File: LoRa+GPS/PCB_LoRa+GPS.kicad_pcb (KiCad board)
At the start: 4 copper layers, 66 parts, among them J1 Conn_Coaxial_Small, J2 USB_C_Receptacle_USB2.0_16P, J4 Conn_Coaxial_Small, Q2 SS8050, Q3 AO3400A, Q4 SS8050, SW1 SW_Push, U1 ESP32-PICO-D4, U2 RFM95W-915S2, U3 TPS62A01ADRL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

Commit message: Add files via upload
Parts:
- added SW2: SW_SPST, Button_Switch_THT:SW_E-Switch_EG1271_SPDT, F.Cu at (85.0, 35.8)
- BT2: moved to B.Cu
- J1: footprint Connector_Coaxial:U.FL_Molex_MCRF_73412-0110_Vertical -> Connector_Coaxial:U.FL_Hirose_U.FL-R-SMT-1_Vertical
- SW1: footprint Button_Switch_SMD:SW_Push_1P1T_NO_Vertical_Wuerth_434133025816 -> Button_Switch_SMD:SW_Push_1P1T_NO_CK_KMR2
- moved Q4 102.1 mm to (61.9, 39.7)
- moved AJ-SR04M1 97.8 mm to (71.0, 36.0)
- moved Q2 87.3 mm to (61.0, 51.1), turned to -90 degrees
- moved U1 83.3 mm to (68.3, 46.3), turned to 180 degrees
- moved Q3 78.1 mm to (77.9, 36.0)
- moved C1 77.5 mm to (82.0, 61.8), turned to -90 degrees
- moved C6 71.9 mm to (69.0, 54.5), turned to -90 degrees
- moved C14 71.9 mm to (79.5, 61.8), turned to -90 degrees
- moved SW1 70.8 mm to (64.0, 60.8), turned to 180 degrees
- moved C4 70.6 mm to (62.5, 54.0)
- moved C11 70.0 mm to (66.5, 54.5), turned to -90 degrees
- moved C9 69.7 mm to (38.5, 43.0), turned to 180 degrees
- moved C15 68.8 mm to (76.9, 61.8), turned to -90 degrees
- moved C2 66.0 mm to (67.8, 54.5), turned to -90 degrees
- moved C3 65.0 mm to (66.5, 57.5), turned to 90 degrees
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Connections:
- BT2 pad 1: +BATT -> Net-(BT2-+)
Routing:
- net 3V3: track 0.00 -> 148.0 mm, vias 0 -> 7
- net GND: track 0.00 -> 76.0 mm, vias 0 -> 9
- net +BATT: track 0.00 -> 60.1 mm, vias 0 -> 1
- net VBUS: track 0.00 -> 53.2 mm, vias 0 -> 2
- net 5V: track 0.00 -> 52.7 mm, vias 0 -> 2
- net PPS_GPS: track 0.00 -> 40.6 mm, vias 0 -> 2
- net Rx_GPS: track 0.00 -> 39.5 mm, vias 0 -> 2
- net Net-(J4-In): track 0.00 -> 37.3 mm
- net Net-(U6-VBUS): track 0.00 -> 36.4 mm, vias 0 -> 3
- net Reset_LoRa: track 0.00 -> 35.6 mm, vias 0 -> 2
- net Tx_GPS: track 0.00 -> 34.4 mm, vias 0 -> 2
- net Net-(U3-SW): track 0.00 -> 33.6 mm, vias 0 -> 2
- net USB_D-: track 0.00 -> 31.6 mm, vias 0 -> 2
- net USB_D+: track 0.00 -> 28.6 mm, vias 0 -> 2
- net RX/TXdone_LoRa: track 0.00 -> 27.3 mm, vias 0 -> 2
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- added copper zone on B.Cu, net GND
- added copper zone on F.Cu, net GND
- added copper zone on In1.Cu, net GND
- added copper zone on In2.Cu, net GND
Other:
- board outline added: 80 x 40 mm

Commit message: Add files via upload
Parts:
- moved C8 25.8 mm to (32.5, 60.5), turned to 90 degrees
- moved C11 11.8 mm to (74.5, 63.3), turned to 90 degrees
- moved C13 11.8 mm to (80.5, 63.3)
- moved C12 11.5 mm to (79.0, 63.3)
- moved C10 11.3 mm to (77.5, 63.3)
- moved C3 11.1 mm to (76.0, 63.3)
- moved C2 10.2 mm to (73.0, 63.3), turned to 90 degrees
- moved R6 10.1 mm to (45.5, 45.0), turned to -90 degrees
- moved C4 9.50 mm to (62.5, 63.5)
- moved C6 9.12 mm to (71.5, 63.3), turned to 90 degrees
- moved R1 8.49 mm to (81.0, 36.0), turned to 90 degrees
- moved R15 5.08 mm to (52.5, 42.0), turned to 90 degrees
- moved R5 4.62 mm to (50.5, 40.5), turned to 0 degrees
- moved C16 4.51 mm to (70.5, 66.5)
- moved C7 4.51 mm to (73.0, 66.4)
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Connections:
- R18 pad 2: +3.3V -> 3V3
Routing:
- net U0TX_uC: track 1.17 -> 80.1 mm, vias 1 -> 3
- net GND: track 76.0 -> 13.1 mm, vias 9 -> 5
- net 3V3: track 148.0 -> 209.8 mm, vias 7 -> 8
- net uC_EN: track 25.0 -> 55.5 mm, vias 2 -> 3
- net Reset_LoRa: track 35.6 -> 57.4 mm, vias 2 -> 3
- net SCK_LoRa: track 19.8 -> 40.8 mm
- net Net-(U6-VBUS): track 36.4 -> 18.0 mm
- net 5V: track 52.7 -> 36.1 mm, vias 2 -> 1
- net NSS_LoRa: track 19.0 -> 34.6 mm
- net RX/TXdone_LoRa: track 27.3 -> 38.6 mm
- net Net-(U3-PG): track 4.72 -> 14.5 mm, vias 0 -> 2
- net U0RX_uC: track 24.3 -> 32.8 mm
- net USB_D+: track 28.6 -> 37.1 mm
- net MOSI_LoRa: track 14.1 -> 21.2 mm
- net Net-(U1-IO2): track 4.13 -> 8.25 mm
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
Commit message: Add files via upload
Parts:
- moved C13 43.8 mm to (38.5, 50.8), turned to 180 degrees
- moved C9 43.2 mm to (81.0, 35.0), turned to -90 degrees
- moved C12 41.9 mm to (38.5, 52.2), turned to 180 degrees
- moved C10 40.1 mm to (38.5, 53.7), turned to 180 degrees
- moved C7 36.4 mm to (52.8, 36.2), turned to 90 degrees
- moved C3 27.5 mm to (66.5, 37.5), turned to 180 degrees
- moved C6 25.9 mm to (68.8, 37.5), turned to 180 degrees
- moved C2 25.4 mm to (66.5, 38.8), turned to 180 degrees
- moved C11 25.2 mm to (68.8, 38.8), turned to 180 degrees
- moved R22 23.1 mm to (68.0, 57.5), turned to -90 degrees
- moved C1 20.2 mm to (100.0, 59.2), turned to 0 degrees
- moved C14 14.2 mm to (74.0, 52.8)
- moved C15 14.0 mm to (72.2, 52.8)
- moved U6 12.6 mm to (44.5, 48.5)
- moved C5 11.8 mm to (49.2, 42.5)
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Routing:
- net U0TX_uC: track 80.1 -> 7.38 mm, vias 3 -> 0
- net Net-(U6-RXD): track 5.60 -> 46.8 mm, vias 0 -> 2
- net USB_D+: track 37.1 -> 12.8 mm, vias 2 -> 0
- net USB_D-: track 33.9 -> 13.2 mm, vias 2 -> 0
- net Net-(U6-TXD): track 7.58 -> 26.1 mm, vias 0 -> 2
- net Net-(Q4-E): track 16.1 -> 31.4 mm
- net Net-(J4-In): track 37.3 -> 51.8 mm
- net Net-(Q2-E): track 18.6 -> 30.0 mm, vias 0 -> 3
- net Net-(Q2-B): track 21.0 -> 9.76 mm
- net GND: track 13.1 -> 22.2 mm, vias 5 -> 8
- net Net-(U4-ISET): track 9.54 -> 2.44 mm
- net Net-(J2-CC2): track 17.1 -> 10.3 mm, vias 0 -> 1
- net Net-(U4-ILIM): track 10.4 -> 3.95 mm
- net Net-(U4-TS): track 10.8 -> 4.64 mm
- net Net-(U4-ITERM): track 9.45 -> 3.44 mm
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
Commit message: Add files via upload
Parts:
- added BT1: 1056TR, CR1220 socket:BAT_1056TR, B.Cu at (75.5, 71.5)
- added R25: 10k, Resistor_SMD:R_0402_1005Metric, F.Cu at (49.5, 69.5)
- moved J4 37.4 mm to (38.5, 73.5)
- moved R24 23.5 mm to (78.5, 61.0), turned to 0 degrees
- moved C19 23.5 mm to (74.5, 44.0), turned to 45 degrees
- moved C4 11.3 mm to (73.5, 61.0)
- moved SW1 10.9 mm to (74.0, 65.2)
- moved R16 8.63 mm to (45.5, 52.0)
- moved CR1 8.44 mm to (32.0, 65.0), turned to -90 degrees
- moved J1 5.59 mm to (94.5, 69.0)
- moved C20 4.40 mm to (57.8, 54.0)
- moved C8 3.16 mm to (31.5, 57.5), turned to 0 degrees
- moved U5 2.28 mm to (49.3, 60.9)
- moved C3 1.44 mm to (65.5, 38.5), turned to 90 degrees
- moved C11 1.25 mm to (70.0, 38.5), turned to 90 degrees
- moved C6 1.06 mm to (68.5, 38.5), turned to 90 degrees
- moved C2 0.53 mm to (67.0, 38.5), turned to 90 degrees
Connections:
- C20 pad 2: Net-(U5-VBATT) -> Net-(U5-VCC)
- J1 pad 1: GND -> Net-(J1-In)
- J1 pad 2: Net-(J1-Ext) -> GND
- L2 pad 2: Net-(U5-VBATT) -> Net-(U5-VCC)
- U1 pad 20: unconnected-(U1-IO13-Pad20) -> Wake_GPS
- U1 pad 42: unconnected-(U1-IO21-Pad42) -> AntOff_GPS
- U2 pad 9: Net-(J1-Ext) -> Net-(J1-In)
- U5 pad 13: unconnected-(U5-ANT_OFF-Pad13) -> AntOff_GPS
- U5 pad 5: unconnected-(U5-Wake-Up-Pad5) -> Wake_GPS
- U5 pad 6: Net-(U5-VBATT) -> VBatt
- U5 pad 7: Net-(U5-VBATT) -> Net-(U5-VCC)
- U5 pad 8: Net-(U5-VBATT) -> Net-(U5-VCC)
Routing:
- net 3V3: track 215.0 -> 77.5 mm
- net AntOff_GPS: track 0.00 -> 56.8 mm, vias 0 -> 2
- net Wake_GPS: track 0.00 -> 52.7 mm, vias 0 -> 2
- net Net-(J4-In): track 51.8 -> 19.2 mm
- net VBatt: track 0.00 -> 24.4 mm, vias 0 -> 3
- net Net-(J1-Ext): track 21.8 -> 0.00 mm
- net PPS_GPS: track 38.4 -> 54.0 mm, vias 2 -> 0
- net Net-(U5-VBATT): track 14.7 -> 0.00 mm
- net Net-(J1-In): track 0.00 -> 11.0 mm
- net GND: track 22.2 -> 12.6 mm, vias 8 -> 59
- net Net-(U5-VCC): track 0.00 -> 9.22 mm
- net Net-(U6-~{RST}): track 11.3 -> 2.17 mm
- net uC_EN: track 55.5 -> 48.6 mm, vias 3 -> 0
- net Tx_GPS: track 38.9 -> 32.9 mm
- net Reset_LoRa: track 57.4 -> 55.1 mm
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- added copper zone on In2.Cu, net 3V3
- removed copper zone on In2.Cu, net GND
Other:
- board size 80 x 40 mm -> 80 x 50 mm

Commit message: V2 +Q1 (Falta DRS)
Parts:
- added Q1: AO3401A, Package_TO_SOT_SMD:SOT-23, B.Cu at (52.5, 53.5)
- added R26: 1k, Resistor_SMD:R_0402_1005Metric, B.Cu at (52.0, 50.5)
- added R27: 10k, Resistor_SMD:R_0402_1005Metric, B.Cu at (54.2, 50.5)
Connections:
- C20 pad 2: Net-(U5-VCC) -> Net-(Q1-S)
- L2 pad 2: Net-(U5-VCC) -> Net-(Q1-S)
- U5 pad 7: Net-(U5-VCC) -> Net-(Q1-D)
- U5 pad 8: Net-(U5-VCC) -> Net-(Q1-D)
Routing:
- net unconnected-(R26-Pad1): track 0.00 -> 20.3 mm, vias 0 -> 1
- net Net-(U5-VCC): track 9.22 -> 0.00 mm
- net (no net): track 0.00 -> 9.22 mm
- net Net-(Q1-D): track 0.00 -> 7.40 mm, vias 0 -> 1
- net Net-(Q1-S): track 0.00 -> 3.69 mm, vias 0 -> 1
- net Pnp_Gps: track 0.00 -> 2.29 mm
- net 3V3: track 77.5 -> 79.0 mm
- net uC_EN: track 48.6 -> 49.2 mm

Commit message: V2 DRC  - Revisar
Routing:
- net (no net): track 9.22 -> 0.00 mm
- net GND: track 12.6 -> 21.1 mm, vias 59 -> 63
- net Net-(Q1-S): track 3.69 -> 11.8 mm
- net Rx_GPS: track 38.3 -> 40.6 mm
- net USB_D-: track 13.2 -> 11.0 mm
- net USB_D+: track 12.8 -> 11.0 mm
- net SCK_LoRa: track 40.8 -> 42.6 mm
- net Net-(D2-K): track 8.96 -> 7.32 mm
- net Reset_LoRa: track 55.1 -> 56.6 mm
- net TRIG_Sensor: track 11.4 -> 10.2 mm
- net Net-(Q1-D): track 7.40 -> 8.50 mm
- net Net-(Q4-E): track 31.4 -> 32.3 mm
- net Net-(U6-TXD): track 26.1 -> 26.9 mm
- net Net-(U4-TS): track 4.64 -> 4.05 mm

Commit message: Varicela y footpads
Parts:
- added TP1: TestPoint, TestPoint:TestPoint_Pad_1.0x1.0mm, F.Cu at (46.5, 67.6)
- added TP10: TestPoint, TestPoint:TestPoint_Pad_1.0x1.0mm, F.Cu at (66.1, 40.3)
- added TP11: TestPoint, TestPoint:TestPoint_Pad_1.0x1.0mm, F.Cu at (76.5, 39.0)
- added TP2: TestPoint, TestPoint:TestPoint_Pad_1.0x1.0mm, F.Cu at (42.0, 44.2)
- added TP3: TestPoint, TestPoint:TestPoint_Pad_1.0x1.0mm, F.Cu at (82.0, 34.6)
- added TP4: TestPoint, TestPoint:TestPoint_Pad_1.0x1.0mm, F.Cu at (56.3, 50.1)
- added TP5: TestPoint, TestPoint:TestPoint_Pad_1.0x1.0mm, F.Cu at (68.3, 40.5)
- added TP6: TestPoint, TestPoint:TestPoint_Pad_1.0x1.0mm, F.Cu at (74.9, 47.1)
- added TP7: TestPoint, TestPoint:TestPoint_Pad_1.0x1.0mm, F.Cu at (73.8, 50.2)
- added TP8: TestPoint, TestPoint:TestPoint_Pad_1.0x1.0mm, B.Cu at (51.9, 56.5)
- added TP9: TestPoint, TestPoint:TestPoint_Pad_1.0x1.0mm, F.Cu at (64.3, 42.3)
- added UCU: LOGO, logos:LogoUCU, F.Cu at (85.4, 65.2)
- moved C16 18.6 mm to (55.5, 47.3), turned to 90 degrees
- moved L2 1.17 mm to (58.2, 51.1)
- moved C9 0.69 mm to (80.3, 35.0)
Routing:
- net Net-(Q1-S): track 11.8 -> 6.04 mm
- net GND: track 21.1 -> 24.0 mm, vias 63 -> 149
- net Net-(Q1-D): track 8.50 -> 6.56 mm
- net 3V3: track 79.4 -> 77.7 mm, vias 8 -> 7
- net MISO_LoRa: track 18.1 -> 19.2 mm
- net +BATT: track 64.0 -> 64.7 mm
- net TRIG_Sensor: track 10.2 -> 10.8 mm
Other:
- board text added: "Sensor V2 28/10/2025 CK, RDT, IR"

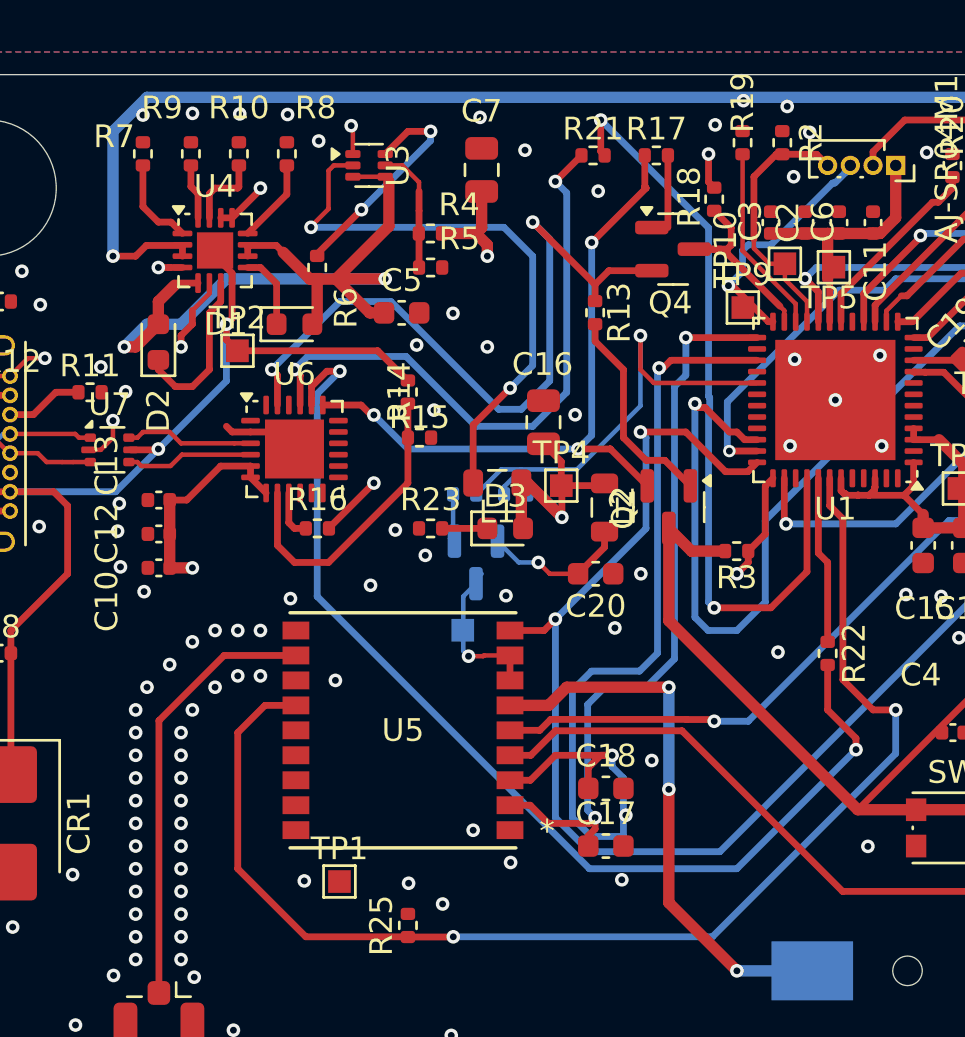
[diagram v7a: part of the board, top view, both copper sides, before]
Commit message: correcciones drc
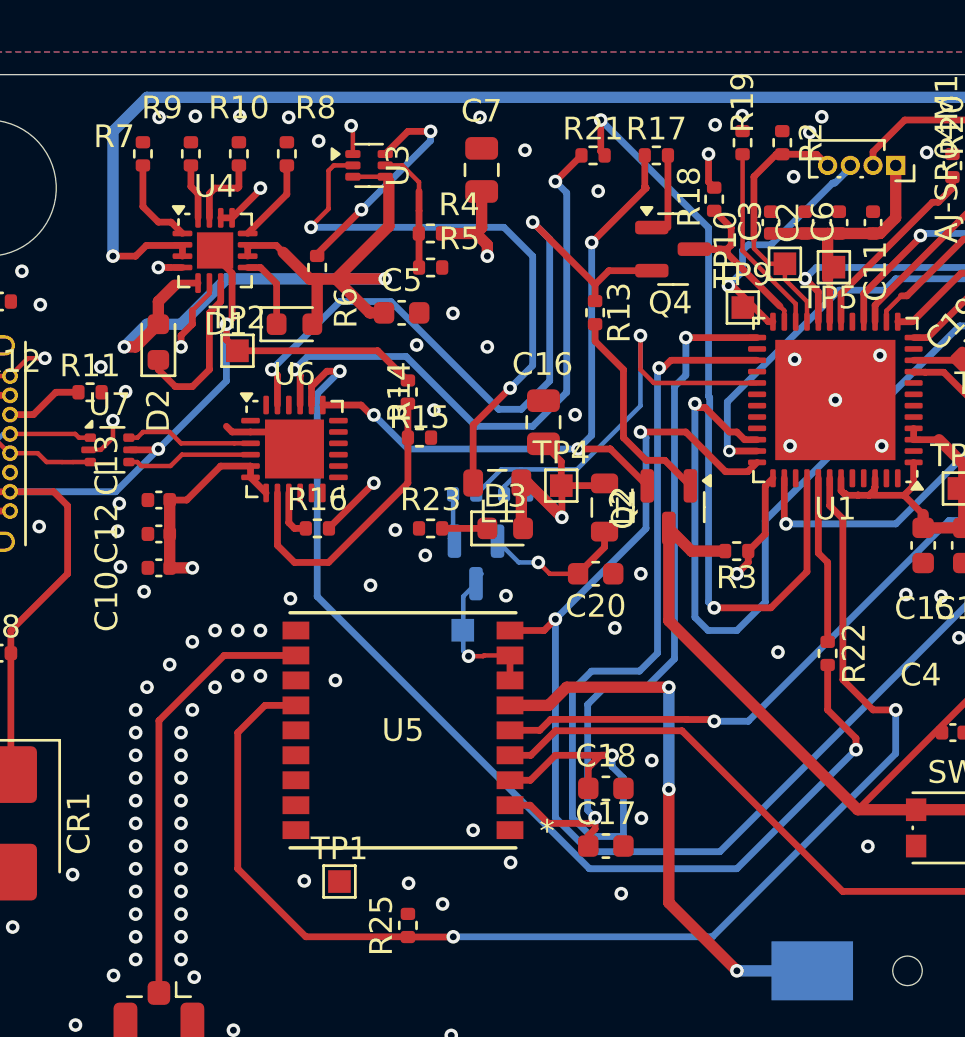
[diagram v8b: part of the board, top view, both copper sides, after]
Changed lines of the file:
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@@
 	)
 	(via
-		(at 44.196 33.7566)
+		(at 44.2468 33.8836)
 		(size 0.6)
 		(drill 0.3)
@@
 	)
 	(via
-		(at 64.2874 33.147)
+		(at 64.2366 33.8074)
 		(size 0.6)
 		(drill 0.3)
@@
 	)
 	(via
-		(at 59.1058 64.643)
+		(at 59.7916 64.77)
 		(size 0.6)
 		(drill 0.3)
@@
 	)
 	(via
-		(at 42.0878 33.7312)
+		(at 42.0878 33.8328)
 		(size 0.6)
 		(drill 0.3)
@@
 	)
 	(via
-		(at 37.8206 33.782)
+		(at 38.5318 33.8836)
 		(size 0.6)
 		(drill 0.3)
@@
 	)
 	(via
-		(at 40.005 33.7058)
+		(at 40.132 33.8328)
 		(size 0.6)
 		(drill 0.3)
@@
 	)
 	(via
-		(at 58.928 67.4878)
+		(at 58.9026 68.0974)
 		(size 0.6)
 		(drill 0.3)
@@
 	)
 	(via
-		(at 66.2178 33.401)
-		(size 0.6)
-		(drill 0.3)
+		(at 67.7418 33.8582)
+		(size 0.6)
+		(drill 0.3)
